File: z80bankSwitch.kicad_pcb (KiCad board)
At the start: 2 copper layers, 123.8 x 87 mm, 28 parts, among them J1 Conn_02x05_Odd_Even, P101 CONN_01X04, P102 CONN_02X20, U1 SST39SF040, U101 7400, U102 Z8400, U105 74LS138, U2 AS6C4008-55PCN, Y101 4MHz

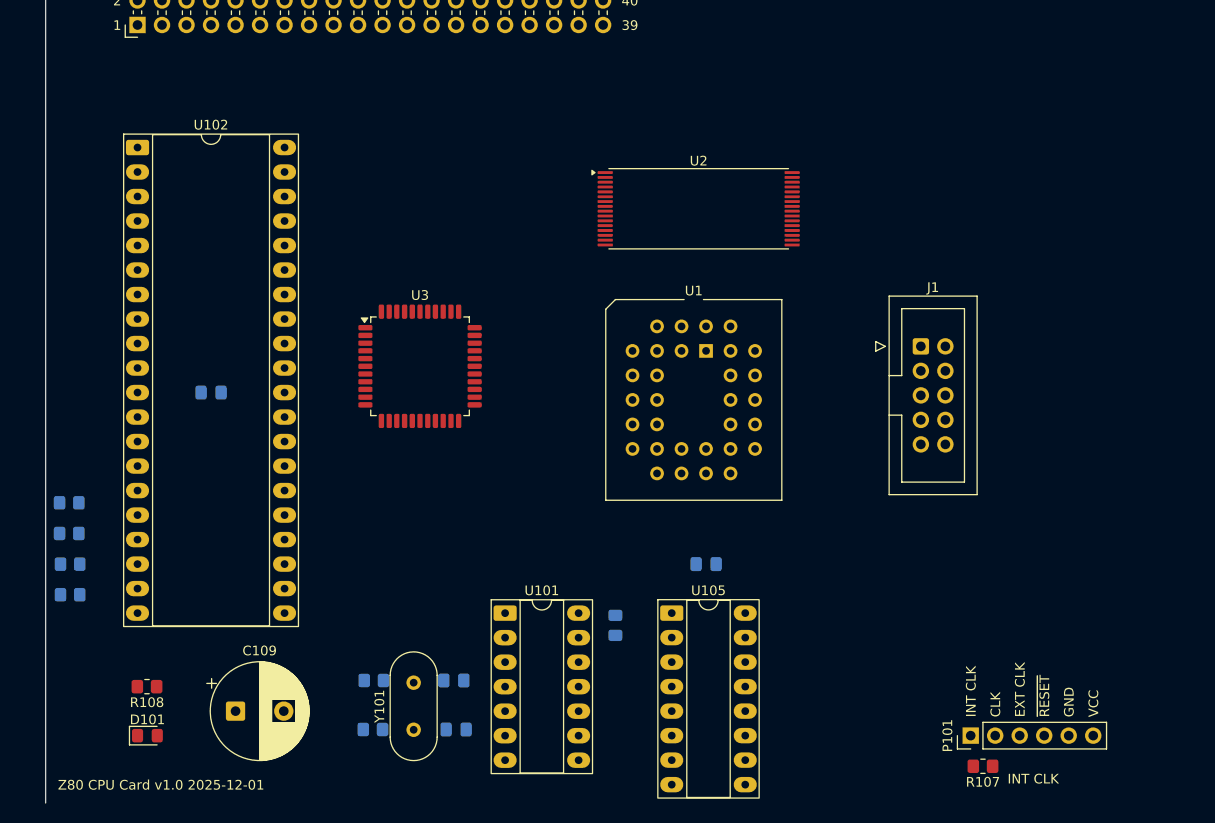
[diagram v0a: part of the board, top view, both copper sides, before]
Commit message: Switch to 1Mx8 SRAM
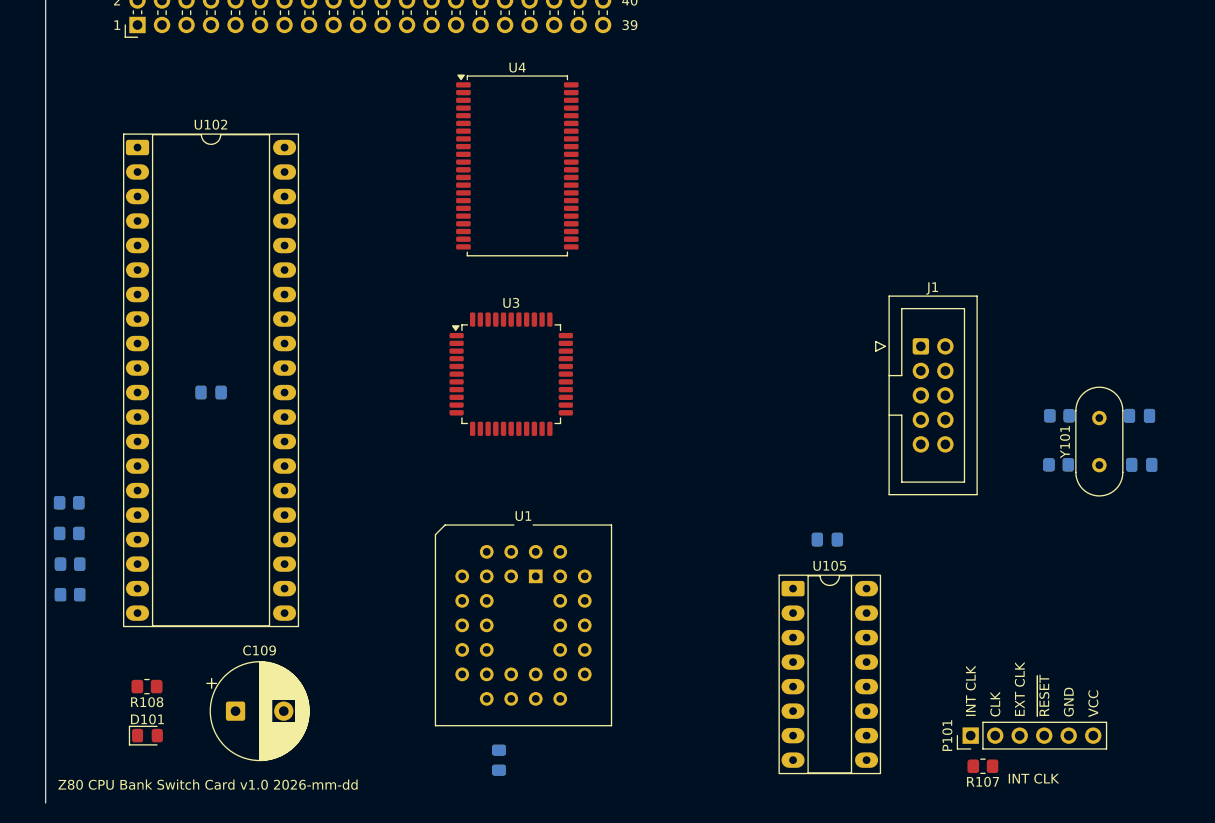
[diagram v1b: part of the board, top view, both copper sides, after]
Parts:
- removed the U101 at (76.2, 215.9)
- removed U2: AS6C4008-55PCN, Package_SO:TSOP-I-32_18.4x8mm_P0.5mm
- added U4: AS6C8008-55ZIN, Package_SO:TSOP-II-44_10.16x18.41mm_P0.8mm, F.Cu at (77.5, 169.5)
- C101, C102, C103, C104, C105: value 0.1u -> C
- C107, C108: value 22pF -> C
- C109: value 10u -> C_Polarized
- P101: value CONN_01X04 -> Conn_01x06_Pin
- P102: value CONN_02X20 -> Conn_02x20_Odd_Even
- R101, R102, R103, R104: value 10k -> R
- R105: value 1M -> R
- R106: value 2k -> R
- R107: value 0 -> R
- R108: value 470 -> R
- U3: value ~ -> EPM3032A
- Y101: value 4MHz -> Crystal
- moved C107 76.2 mm to (142.2, 200.5)
- moved R105 76.2 mm to (133.6, 200.5)
- moved R106 76.2 mm to (133.7, 195.5)
- moved C108 76.2 mm to (142.0, 195.5)
- moved Y101 76.2 mm to (137.8, 200.6)
- moved U1 29.3 mm to (79.4, 212.1)
- moved C101 18.5 mm to (75.6, 231.1)
- moved U105 12.8 mm to (106.0, 213.4)
- moved C105 12.8 mm to (109.6, 208.3)
- moved U3 9.49 mm to (76.8, 191.1)
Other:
- board text added: "Z80 CPU Bank Switch Card v1.0 2026-mm-dd"
- board text removed: "Z80 CPU Card v1.0 2025-12-01"

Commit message: Much routing
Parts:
- removed P101: Conn_01x06_Pin, Connector_PinHeader_2.54mm:PinHeader_1x06_P2.54mm_Vertical
- removed the U3 at (76.8, 191.1)
- added C10: 100n, Capacitor_SMD:C_0805_2012Metric_Pad1.18x1.45mm_HandSolder, F.Cu at (77.2, 201.7)
- added C11: 100n, Capacitor_SMD:C_0805_2012Metric_Pad1.18x1.45mm_HandSolder, B.Cu at (86.9, 193.3)
- added C12: 100n, Capacitor_SMD:C_0805_2012Metric_Pad1.18x1.45mm_HandSolder, B.Cu at (68.8, 192.5)
- added C5: 100n, Capacitor_SMD:C_0805_2012Metric_Pad1.18x1.45mm_HandSolder, F.Cu at (125.1, 167.1)
- added C7: 100n, Capacitor_SMD:C_0805_2012Metric_Pad1.18x1.45mm_HandSolder, F.Cu at (125.1, 170.1)
- added C9: 100n, Capacitor_SMD:C_0805_2012Metric_Pad1.18x1.45mm_HandSolder, F.Cu at (78.0, 183.1)
- added U2: MCP1700x-300xxTT, Package_TO_SOT_SMD:SOT-23, F.Cu at (130.0, 182.2)
- added U5: EPM3032A Z80 Bank Switcher, Package_QFP:TQFP-44_10x10mm_P0.8mm, F.Cu at (77.7, 192.5)
- C4: renamed from C109; value C_Polarized -> 10u
- J1: value Conn_02x05_Odd_Even -> Altera JTAG 10pin Male Connector
- U3: renamed from U102; footprint Package_DIP:DIP-40_W15.24mm_Socket_LongPads -> Package_DIP:DIP-40_W15.24mm_Socket
- moved J1 16.8 mm to (116.0, 171.7)
- renumbered C107 to C1, C104 to C13, C103 to C14, C101 to C2, C108 to C3, C102 to C6, C105 to C8, D101 to D1, P102 to P1, R105 to R1, R106 to R2, R107 to R3, R108 to R4, R101 to R5, R102 to R6, R103 to R7, R104 to R8, U101 to U1, U105 to U4, U4 to U6, U1 to U7, Y101 to Y1
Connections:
- C1 pad 1: Net-(C107-Pad1) -> Net-(C1-Pad1)
- J1 pad 1: unconnected-(J1-Pin_1-Pad1) -> /TCK
- J1 pad 10: unconnected-(J1-Pin_10-Pad10) -> GND
- J1 pad 2: unconnected-(J1-Pin_2-Pad2) -> GND
- J1 pad 3: unconnected-(J1-Pin_3-Pad3) -> /TDO
- J1 pad 4: unconnected-(J1-Pin_4-Pad4) -> +3.3V
- J1 pad 5: unconnected-(J1-Pin_5-Pad5) -> /TMS
- J1 pad 9: unconnected-(J1-Pin_9-Pad9) -> /TDI
- R1 pad 2: Net-(C107-Pad1) -> Net-(C1-Pad1)
- U1 pad 1: (no net) -> Net-(C1-Pad1)
- U1 pad 10: Net-(C107-Pad1) -> GND
- U1 pad 2: (no net) -> Net-(C1-Pad1)
- U1 pad 3: (no net) -> /CLK_INT
- U1 pad 4: (no net) -> GND
- U1 pad 5: (no net) -> GND
- U1 pad 6: (no net) -> unconnected-(U1-Pad6)
- U1 pad 8: /CLK_INT -> unconnected-(U1-Pad8)
- U1 pad 9: Net-(C107-Pad1) -> GND
- U4 pad 11: unconnected-(U105-O4-Pad11) -> /~{CPLD_CE}
- U6 pad 18: unconnected-(U4-A19-Pad18) -> /A19_OUT
- U6 pad 19: unconnected-(U4-A18-Pad19) -> /A18_OUT
- U6 pad 20: unconnected-(U4-A17-Pad20) -> /A17_OUT
- U6 pad 21: unconnected-(U4-A16-Pad21) -> /A16_OUT
- U6 pad 22: unconnected-(U4-A15-Pad22) -> /A15_OUT
- U6 pad 23: unconnected-(U4-A14-Pad23) -> /A14_OUT
- U6 pad 24: unconnected-(U4-A13-Pad24) -> A13
- U6 pad 40: unconnected-(U4-CE2-Pad40) -> VCC
- U7 pad 1: unconnected-(U1-A18-Pad1) -> /A18_OUT
- U7 pad 2: unconnected-(U1-A16-Pad2) -> /A16_OUT
- U7 pad 28: unconnected-(U1-A13-Pad28) -> A13
- U7 pad 29: unconnected-(U1-A14-Pad29) -> /A14_OUT
- U7 pad 3: unconnected-(U1-A15-Pad3) -> /A15_OUT
- U7 pad 30: unconnected-(U1-A17-Pad30) -> /A17_OUT
- Y1 pad 1: Net-(C107-Pad1) -> Net-(C1-Pad1)
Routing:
- net ~{MREQ}: track 0.00 -> 159.2 mm, vias 0 -> 6
- net D0: track 0.00 -> 151.0 mm, vias 0 -> 3
- net A7: track 0.00 -> 143.3 mm, vias 0 -> 5
- net A6: track 0.00 -> 135.8 mm, vias 0 -> 4
- net ~{IORQ}: track 0.00 -> 133.3 mm, vias 0 -> 3
- net A5: track 0.00 -> 131.2 mm, vias 0 -> 3
- net A4: track 0.00 -> 126.3 mm, vias 0 -> 3
- net D5: track 0.00 -> 107.0 mm, vias 0 -> 3
- net D4: track 0.00 -> 100.5 mm, vias 0 -> 2
- net A14: track 0.00 -> 97.7 mm, vias 0 -> 3
- net A15: track 0.00 -> 93.6 mm, vias 0 -> 3
- net A0: track 0.00 -> 92.4 mm, vias 0 -> 6
- net D6: track 0.00 -> 86.1 mm, vias 0 -> 1
- net D3: track 0.00 -> 80.3 mm, vias 0 -> 3
- net /~{CPLD_CE}: track 0.00 -> 79.4 mm, vias 0 -> 2
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
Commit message: pcb routing almost full
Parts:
- R3: moved to B.Cu
- moved C13 166.1 mm to (112.4, 192.1)
- moved C14 166.1 mm to (112.4, 189.1)
- moved U1 138.6 mm to (96.5, 160.0)
- moved R3 75.0 mm to (92.7, 164.5), turned to 0 degrees
- moved C2 68.2 mm to (100.3, 167.6)
- moved C3 64.9 mm to (93.3, 152.4), turned to 180 degrees
- moved C1 61.0 mm to (104.8, 152.4)
- moved Y1 60.3 mm to (101.5, 152.4), turned to 180 degrees
- moved R1 56.6 mm to (93.3, 160.7), turned to 90 degrees
- moved R2 55.2 mm to (90.8, 160.7), turned to 90 degrees
- moved J1 46.7 mm to (98.9, 215.3)
- moved C7 42.8 mm to (97.2, 202.6), turned to -90 degrees
- moved C5 41.5 mm to (103.5, 202.6), turned to 90 degrees
- moved U2 36.2 mm to (100.4, 203.0), turned to -90 degrees
- moved U4 34.4 mm to (96.5, 180.3)
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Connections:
- net /CLK_INT renamed Net-(R1-Pad1)
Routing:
- net GND: track 36.6 -> 312.4 mm, vias 6 -> 17
- net VCC: track 6.58 -> 232.3 mm, vias 0 -> 11
- net ~{RESET}: track 0.00 -> 93.7 mm, vias 0 -> 4
- net ~{BUSREQ}: track 0.00 -> 92.7 mm, vias 0 -> 3
- net ~{INT}: track 0.00 -> 88.2 mm, vias 0 -> 2
- net ~{WAIT}: track 0.00 -> 85.9 mm, vias 0 -> 1
- net A9: track 33.2 -> 116.9 mm, vias 1 -> 6
- net A10: track 37.0 -> 120.8 mm, vias 1 -> 4
- net A3: track 45.5 -> 124.9 mm, vias 1 -> 4
- net ~{BUSACK}: track 0.00 -> 78.7 mm, vias 0 -> 3
- net A2: track 58.9 -> 135.4 mm, vias 4 -> 6
- net D6: track 86.1 -> 156.7 mm, vias 1 -> 4
- net ~{WR}: track 54.3 -> 123.6 mm, vias 1 -> 4
- net ~{SIO_CE}: track 0.00 -> 55.7 mm, vias 0 -> 2
- net +3.3V: track 17.9 -> 73.5 mm, vias 2 -> 4
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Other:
- board text removed: "CLK"
- board text removed: "EXT CLK"
- board text removed: "GND"
- board text removed: "INT CLK"
- board text removed: "VCC"
- board text removed: "~{RESET}"

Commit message: All connected
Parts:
- C13, C14: moved to B.Cu
- moved C14 56.7 mm to (72.9, 229.7), turned to 180 degrees
- moved C13 41.7 mm to (77.2, 169.7), turned to 90 degrees
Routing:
- net A8: track 53.7 -> 138.7 mm, vias 3 -> 6
- net VCC: track 232.3 -> 303.7 mm, vias 11 -> 14
- net GND: track 312.4 -> 376.9 mm, vias 17 -> 20
- net /TDI: track 5.66 -> 68.8 mm, vias 1 -> 3
- net A13: track 70.4 -> 133.1 mm, vias 4 -> 8
- net A12: track 76.7 -> 134.7 mm, vias 3 -> 4
- net /TMS: track 3.28 -> 60.4 mm, vias 1 -> 3
- net A11: track 88.1 -> 142.6 mm, vias 4 -> 7
- net /A17_OUT: track 23.8 -> 71.8 mm, vias 1 -> 5
- net /A16_OUT: track 26.2 -> 69.3 mm, vias 1 -> 5
- net /A14_OUT: track 16.8 -> 58.7 mm, vias 0 -> 4
- net D3: track 123.9 -> 164.4 mm, vias 4 -> 7
- net D1: track 121.1 -> 158.4 mm, vias 2 -> 6
- net /TCK: track 3.71 -> 37.1 mm
- net /TDO: track 15.6 -> 45.7 mm, vias 1 -> 3
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
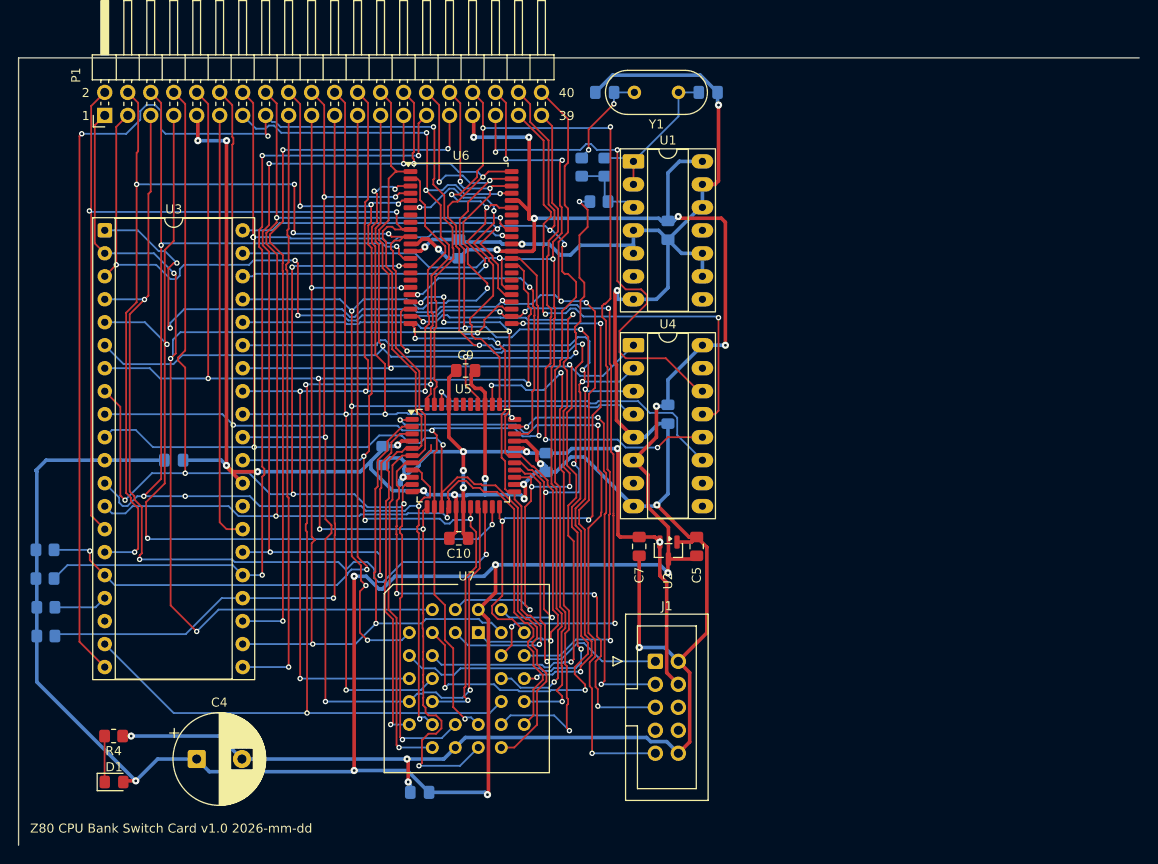
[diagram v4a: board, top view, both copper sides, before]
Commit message: PCB Routing complete
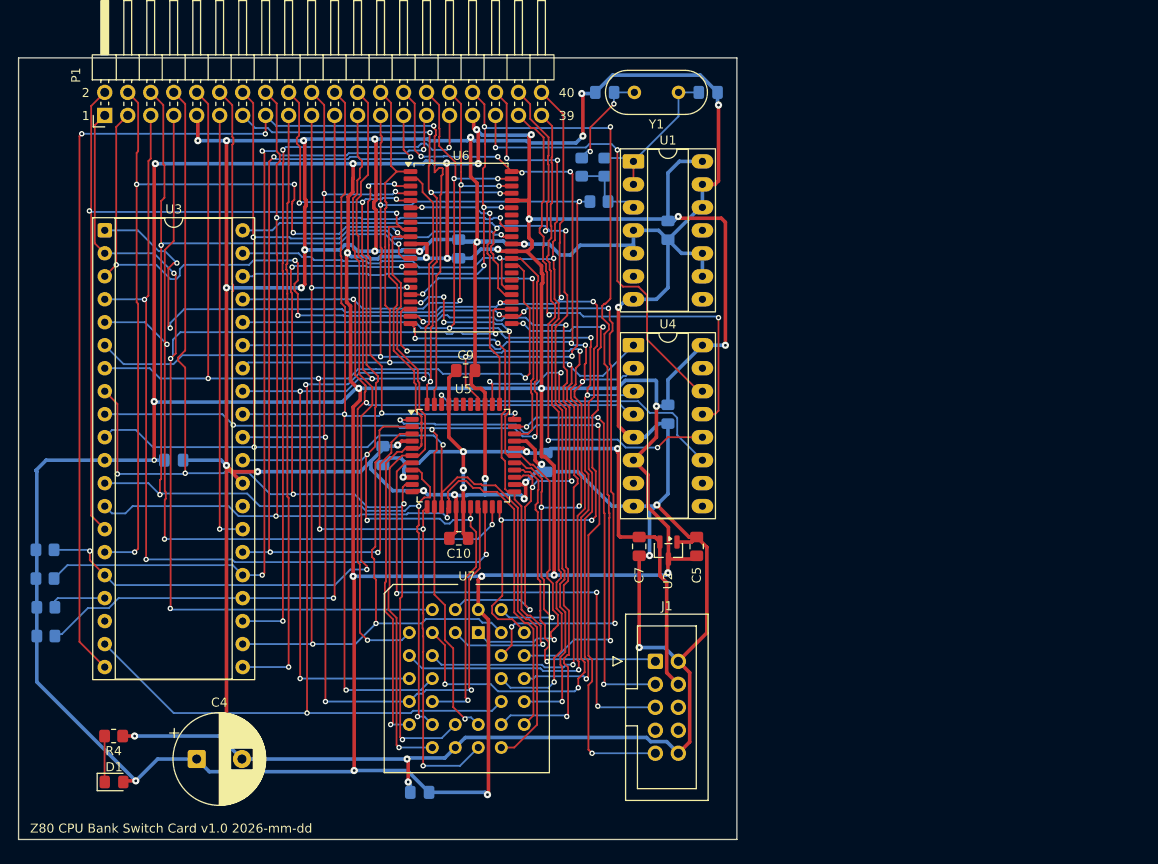
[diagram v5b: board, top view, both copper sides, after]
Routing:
- net VCC: track 303.7 -> 534.6 mm, vias 14 -> 25
- net GND: track 376.9 -> 536.9 mm, vias 20 -> 32
- net CLK: track 106.0 -> 126.4 mm, vias 4 -> 5
- net A6: track 146.5 -> 139.4 mm
- net /~{CE_RAM}: track 37.4 -> 30.8 mm
- net ~{CTC_CE}: track 55.1 -> 48.8 mm
- net A7: track 133.8 -> 128.0 mm, vias 7 -> 6
- net A8: track 138.7 -> 133.3 mm
- net ~{IORQ}: track 139.6 -> 134.4 mm
- net A14: track 102.3 -> 97.2 mm
- net +3.3V: track 87.8 -> 83.3 mm, vias 7 -> 6
- net ~{RESET}: track 99.2 -> 94.8 mm
- net D4: track 161.5 -> 157.7 mm
- net /TMS: track 60.4 -> 56.8 mm
- net D3: track 164.4 -> 160.9 mm
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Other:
- board size 123.8 x 87 mm -> 79.4 x 86.4 mm

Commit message: v1.0 completed
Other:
- board text added: "Z80 CPU Bank Switch Card v1.0 2026-09-16"
- board text removed: "Z80 CPU Bank Switch Card v1.0 2026-mm-dd"
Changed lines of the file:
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@@
 		(layer "Edge.Cuts")
 	)
-	(gr_text "Z80 CPU Bank Switch Card v1.0 2026-mm-dd"
+	(gr_text "Z80 CPU Bank Switch Card v1.0 2026-09-16"
 		(at 29.845 234.315 0)
 		(layer "F.SilkS")
